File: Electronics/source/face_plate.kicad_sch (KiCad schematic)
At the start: 13 parts, among them J19 Conn_01x08, J20 Conn_01x03, SW1 SW_Push, SW16 SW_Push, SW17 SKRHABE010

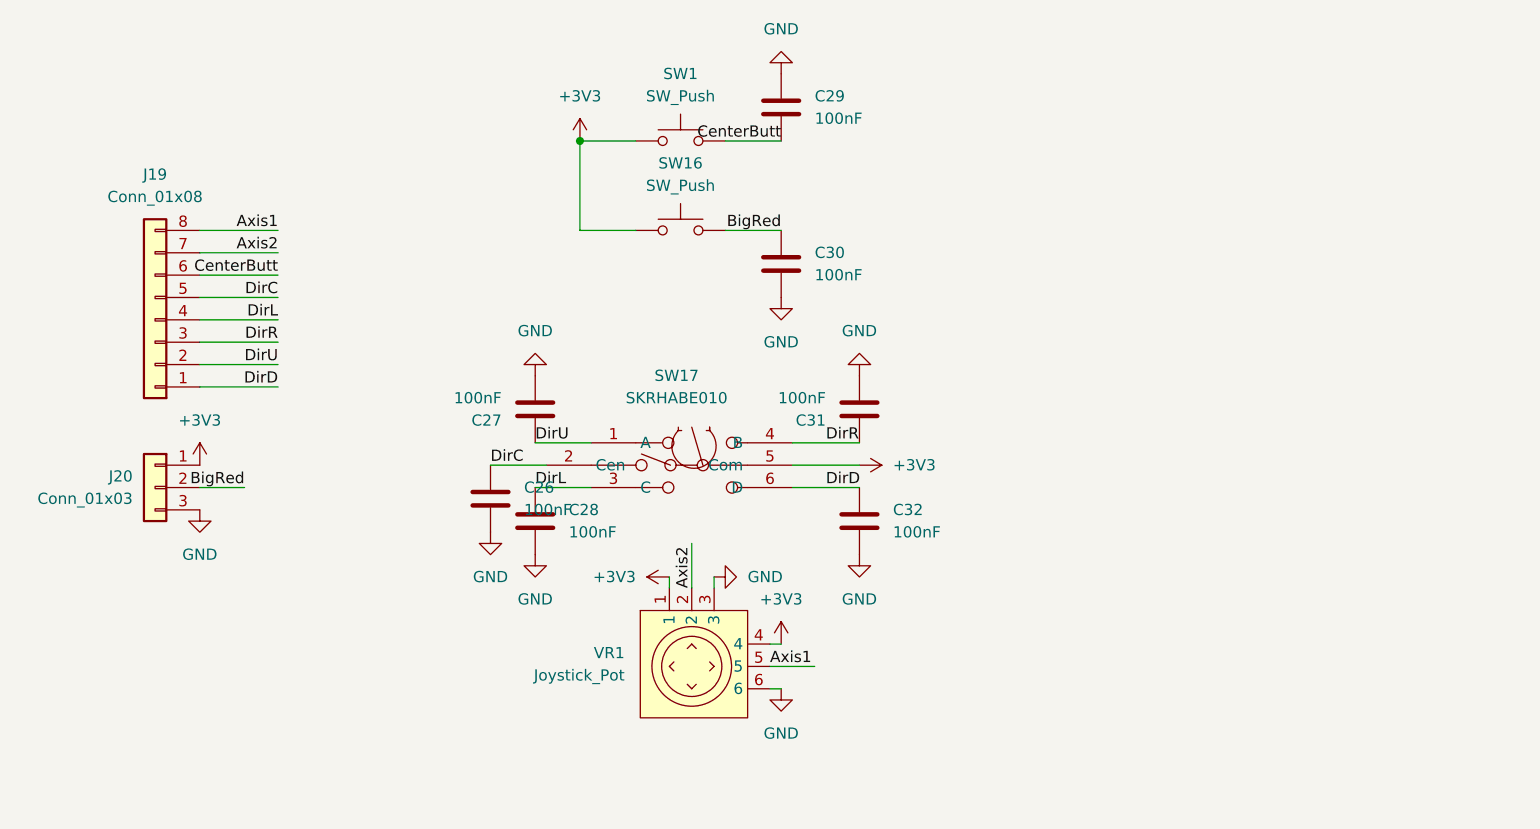
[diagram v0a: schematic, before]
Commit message: Redefined face shape to fit panel mount hat; rerouted; DRC check
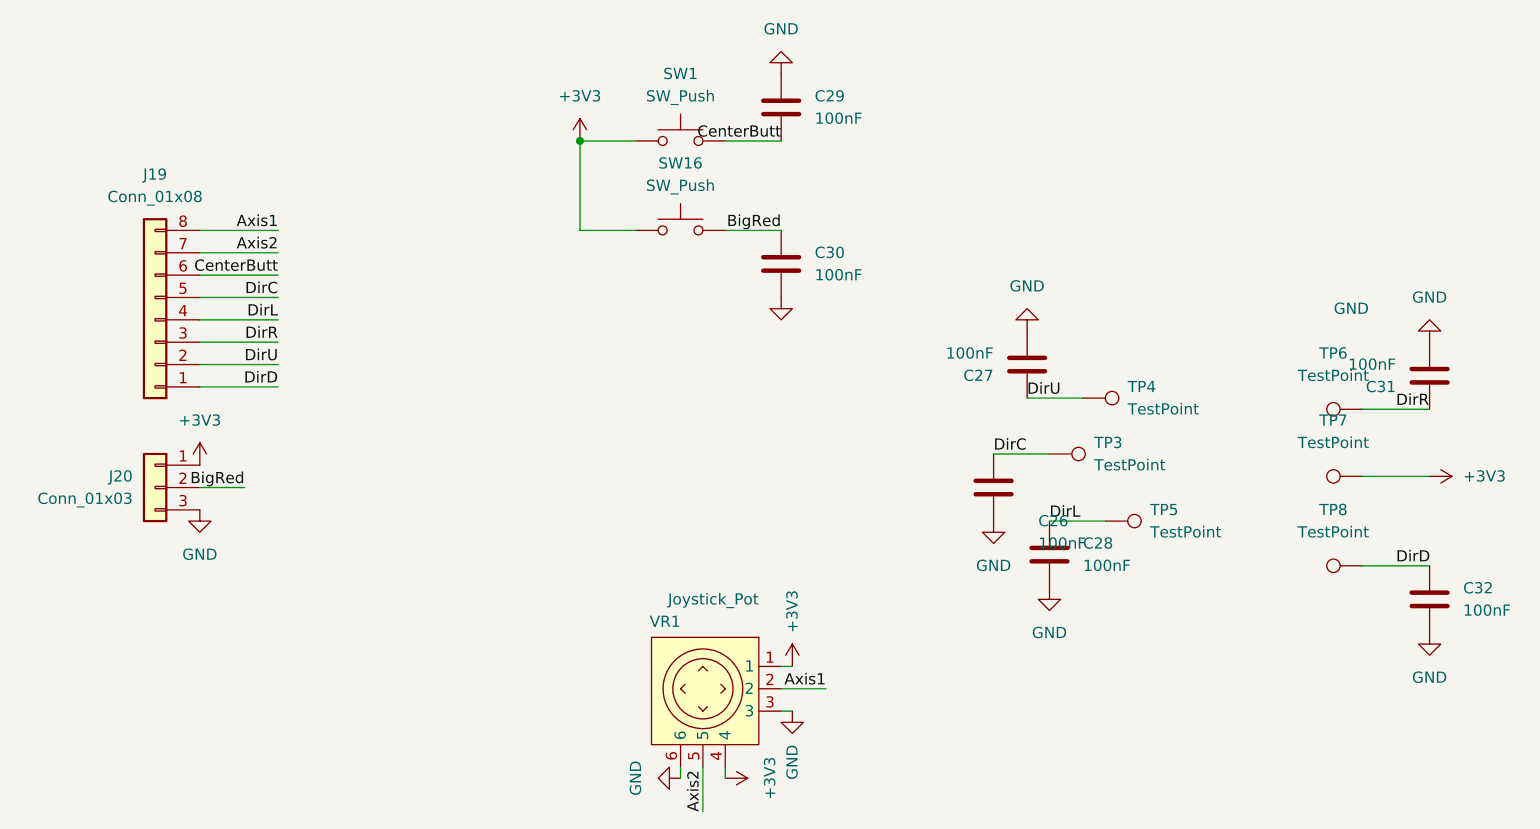
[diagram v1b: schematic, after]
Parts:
- removed SW17: SKRHABE010, Personal:SKRHABE010, symbol Personal:SKRHABE010
- added TP3, TP4, TP5, TP6, TP7, TP8: TestPoint, TestPoint:TestPoint_Loop_D1.80mm_Drill1.0mm_Beaded, symbol Connector:TestPoint
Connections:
- net +3V3: now also TP7.1
- net Axis1: now also VR1.2; no longer VR1.5
- net Axis2: now also VR1.5; no longer VR1.2
- net DirC: now also TP3.1
- net DirD: now also TP8.1
- net DirL: now also TP5.1
- net DirR: now also TP6.1
- net DirU: now also TP4.1
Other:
- moved on the sheet: C26, C27, C28, C31, C32, VR1
